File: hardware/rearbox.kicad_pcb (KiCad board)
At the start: 2 copper layers, 120 x 60 mm, 4 parts

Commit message: Add components
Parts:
- added G***: LOGO, Local_Library:putm_text_30mm, F.Cu at (203.0, 103.0)
- added REF**: MountingHole_3mm_Pad_Via, MountingHole:MountingHole_3mm_Pad_Via, F.Cu at (148.0, 129.0)
- added REF**: MountingHole_3mm_Pad_Via, MountingHole:MountingHole_3mm_Pad_Via, F.Cu at (148.0, 79.0)
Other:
- copper layers 2 -> 4
- board text added: "v${REVISION}"
- board text removed: "Rev: ${REVISION}"

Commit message: Add the Cube project
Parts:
- G***: footprint Local_Library:putm_text_30mm -> Local_Library:PUTM_TEXT_30MM
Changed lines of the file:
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@@
     (pad "1" thru_hole circle locked (at 2.25 0) (size 0.8 0.8) (drill 0.5) (layers "*.Cu" "*.Mask"))
   )
-  (footprint "Local_Library:putm_text_30mm" (layer "F.Cu")
+  (footprint "Local_Library:PUTM_TEXT_30MM" (layer "F.Cu")
     (at 203 103 90)
     (attr board_only exclude_from_pos_files exclude_from_bom)

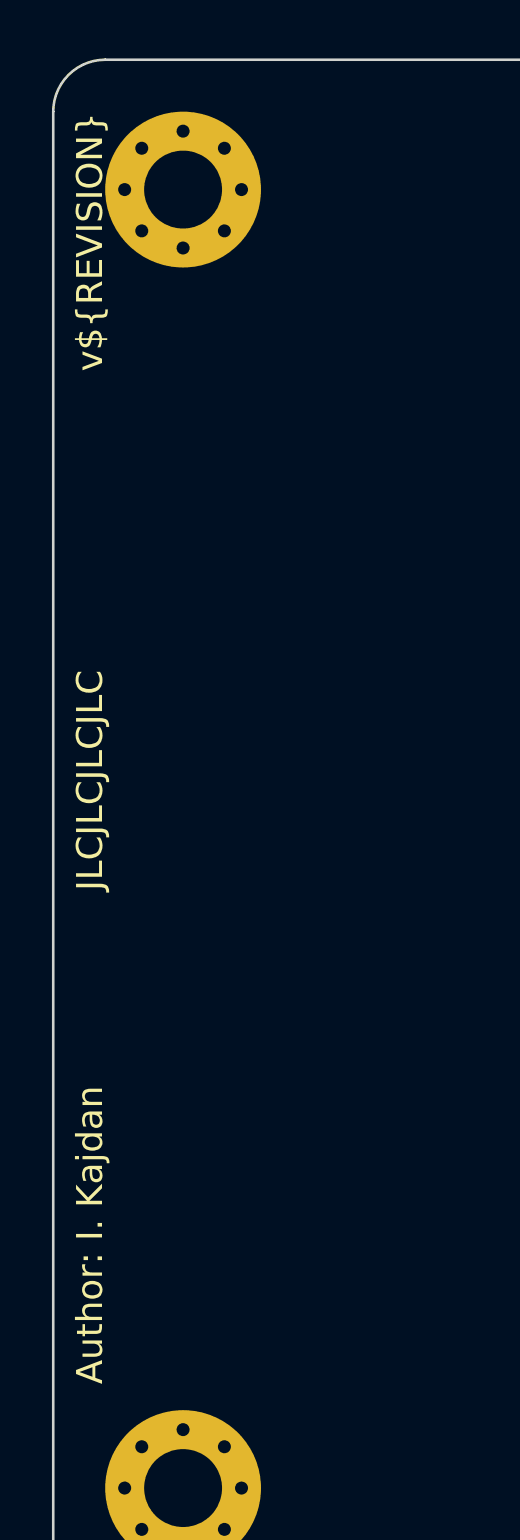
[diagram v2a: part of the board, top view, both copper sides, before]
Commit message: Improve the diagram based on the feedback
- add an input LC filter
- remove the USB connector
- add a programmer connector
- move optocouplers into a subsheet
- add a suspension tension meter IC
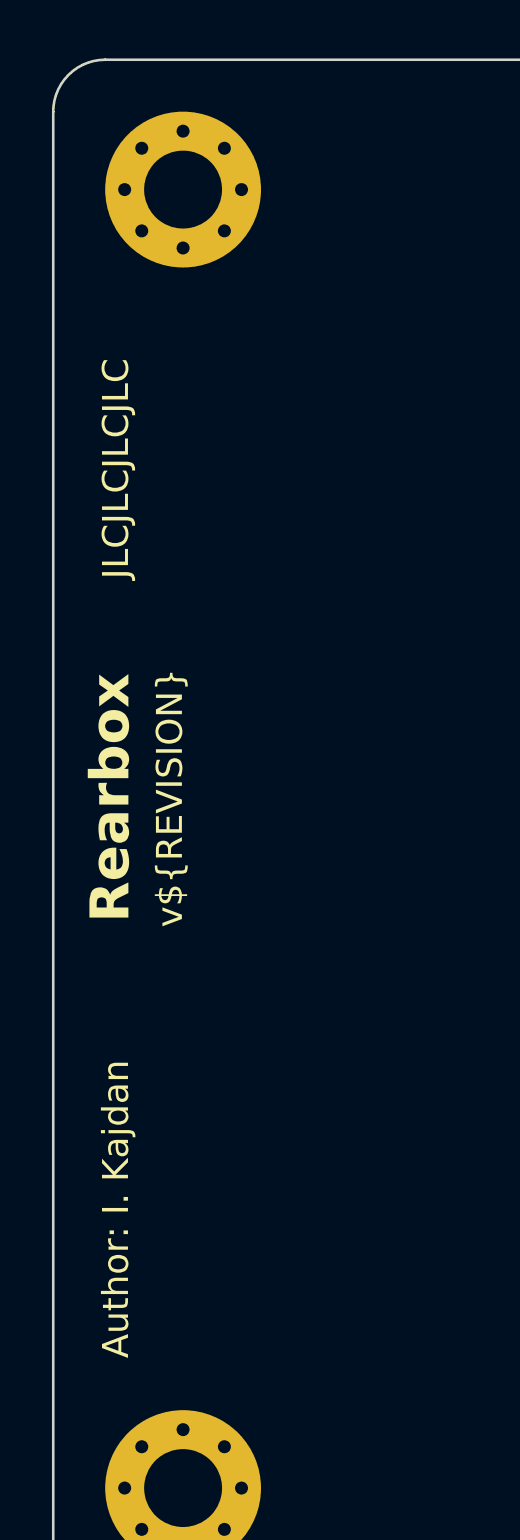
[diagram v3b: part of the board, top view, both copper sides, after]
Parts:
- removed the G*** at (203.0, 103.0)
- added G***: LOGO, Local_Library:PUTM_Logo_Text_30mm, F.Cu at (203.0, 103.0)
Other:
- board text added: "Rearbox"
